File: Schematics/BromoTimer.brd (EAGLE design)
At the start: 49.2 x 71.1 mm, 27 parts, among them IC1 PIC16F687, IC2 7805TV, K1 351, K2 351, Q1 2N3565, Q2 2N3565, Q3 2N3565, X4 22-23-2031, X5 BUZZER

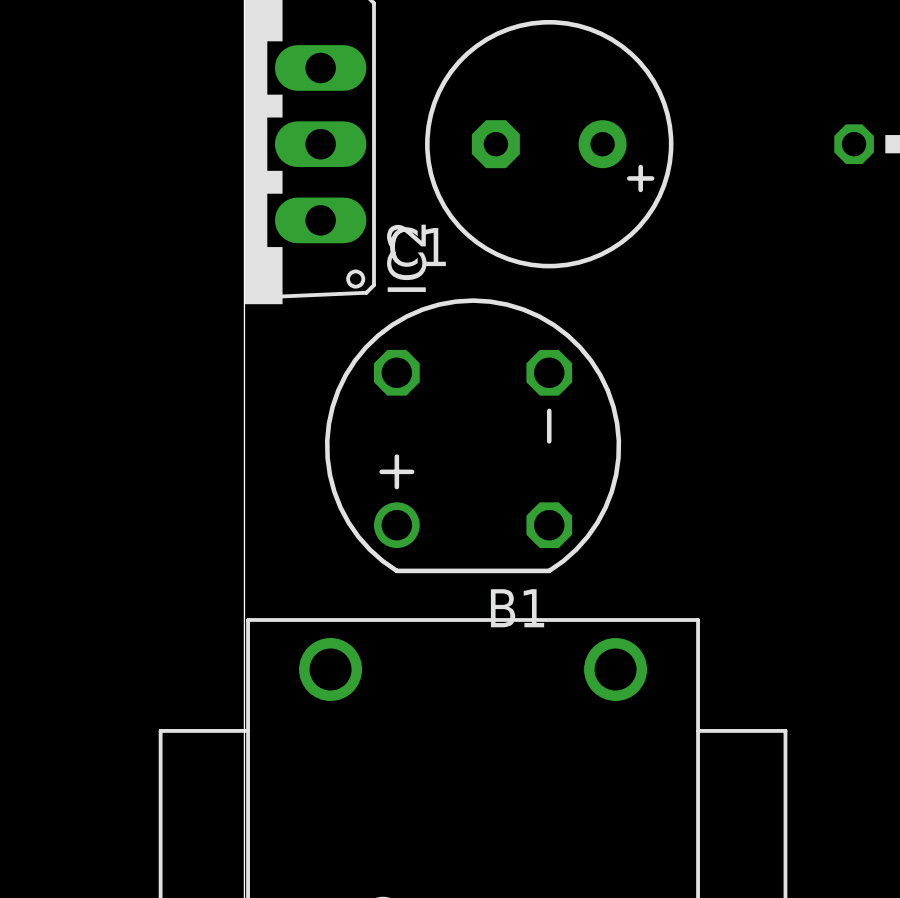
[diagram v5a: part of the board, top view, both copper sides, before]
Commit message: Add 1n4004 diode
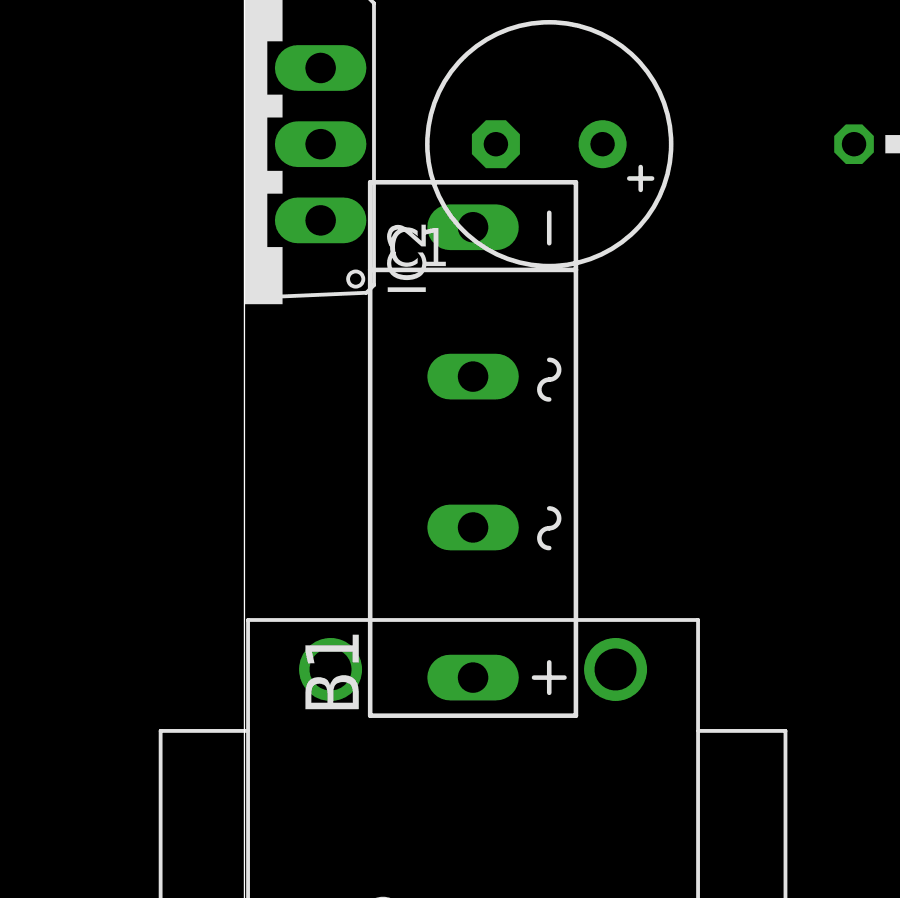
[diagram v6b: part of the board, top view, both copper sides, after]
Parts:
- B1: device rectifier:RB1A -> rectifier:2KBB-R
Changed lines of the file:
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@@
 </element>
 <element name="U$1" library="SparkFun" package="TRANSFORMER" value="TRANSFORMERPTH" x="7.62" y="19.05" rot="R90"/>
-<element name="B1" library="rectifier" package="RB1A" value="" x="7.62" y="31.75" rot="R90"/>
+<element name="B1" library="rectifier" package="2KBB-R" value="" x="7.62" y="31.75" rot="R90"/>
 <element name="D1" library="diode" package="DO35-7" value="1N4148DO35-7" x="3.81" y="-6.35"/>
 <element name="D2" library="diode" package="DO35-7" value="1N4148DO35-7" x="3.81" y="-12.7"/>
@@
 <wire x1="44.45" y1="36.83" x2="42.545" y2="50.8" width="0" layer="19" extent="1-1"/>
 <wire x1="29.21" y1="36.83" x2="44.45" y2="36.83" width="0" layer="19" extent="1-1"/>
-<wire x1="10.16" y1="34.29" x2="29.21" y2="36.83" width="0" layer="19" extent="1-1"/>
-<wire x1="8.382" y1="41.91" x2="10.16" y2="34.29" width="0" layer="19" extent="1-1"/>
+<wire x1="7.62" y1="39.1414" x2="29.21" y2="36.83" width="0" layer="19" extent="1-1"/>
+<wire x1="8.382" y1="41.91" x2="7.62" y2="39.1414" width="0" layer="19" extent="1-1"/>
 <wire x1="2.54" y1="41.91" x2="8.382" y2="41.91" width="0" layer="19" extent="1-1"/>
 <wire x1="5.08" y1="50.8" x2="2.54" y2="41.91" width="0" layer="19" extent="1-1"/>
@@
 <wire x1="19.05" y1="67.31" x2="12.7" y2="52.07" width="0" layer="19" extent="1-1"/>
 <wire x1="2.54" y1="67.31" x2="19.05" y2="67.31" width="0" layer="19" extent="1-1"/>
-<wire x1="7.62" y1="-6.35" x2="10.16" y2="34.29" width="0" layer="19" extent="1-1"/>
+<wire x1="7.62" y1="-6.35" x2="7.62" y2="39.1414" width="0" layer="19" extent="1-1"/>
 <wire x1="7.62" y1="-12.7" x2="7.62" y2="-6.35" width="0" layer="19" extent="1-1"/>
 <wire x1="5.08" y1="-20.32" x2="7.62" y2="-12.7" width="0" layer="19" extent="1-1"/>
@@
 <contactref element="U$1" pad="3"/>
 <contactref element="B1" pad="AC2"/>
-<wire x1="12.37" y1="24.4" x2="10.16" y2="29.21" width="0" layer="19" extent="1-1"/>
+<wire x1="12.37" y1="24.4" x2="7.62" y2="34.163" width="0" layer="19" extent="1-1"/>
 </signal>
 <signal name="N$12">
 <contactref element="B1" pad="AC1"/>
 <contactref element="U$1" pad="4"/>
-<wire x1="2.87" y1="24.4" x2="5.08" y2="34.29" width="0" layer="19" extent="1-1"/>
+<wire x1="2.87" y1="24.4" x2="7.62" y2="29.1338" width="0" layer="19" extent="1-1"/>
 </signal>
 <signal name="V+">
@@
 <wire x1="11.938" y1="41.91" x2="26.67" y2="31.75" width="0" layer="19" extent="1-1"/>
 <wire x1="2.54" y1="39.37" x2="11.938" y2="41.91" width="0" layer="19" extent="1-1"/>
-<wire x1="5.08" y1="29.21" x2="2.54" y2="39.37" width="0" layer="19" extent="1-1"/>
-<wire x1="0" y1="-6.35" x2="5.08" y2="29.21" width="0" layer="19" extent="1-1"/>
+<wire x1="7.62" y1="24.13" x2="2.54" y2="39.37" width="0" layer="19" extent="1-1"/>
+<wire x1="0" y1="-6.35" x2="7.62" y2="24.13" width="0" layer="19" extent="1-1"/>
 <wire x1="0" y1="-12.7" x2="0" y2="-6.35" width="0" layer="19" extent="1-1"/>
 <wire x1="0" y1="-27.94" x2="0" y2="-12.7" width="0" layer="19" extent="1-1"/>

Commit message: Fix bug in relay protection
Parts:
- D3: value 1N4148DO35-7 -> 1N4004; device diode:DO35-7 -> diode:DO41-10
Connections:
- net GND: no longer D1.A, D2.A
- net N$6: now also D1.A
- net N$7: now also D2.A
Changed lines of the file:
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@@
 <attribute name="OC_FARNELL" value="unknown" x="5.08" y="-20.32" size="1.778" layer="27" display="off"/>
 </element>
-<element name="D3" library="diode" package="DO35-7" value="1N4148DO35-7" x="3.81" y="-27.94"/>
+<element name="D3" library="diode" package="DO41-10" value="1N4004" x="3.81" y="-27.94"/>
 <element name="Q3" library="transistor-npn" package="TO92" value="2N3565" x="0" y="-34.29"/>
 <element name="R5" library="rcl" package="0207/10" value="" x="3.81" y="-39.37"/>
@@
 <wire x1="2.54" y1="44.45" x2="2.54" y2="50.8" width="0" layer="19" extent="1-1"/>
 <wire x1="2.54" y1="-20.32" x2="2.54" y2="44.45" width="0" layer="19" extent="1-1"/>
-<wire x1="7.62" y1="-27.94" x2="2.54" y2="-20.32" width="0" layer="19" extent="1-1"/>
+<wire x1="8.89" y1="-27.94" x2="2.54" y2="-20.32" width="0" layer="19" extent="1-1"/>
 </signal>
 <signal name="GND">
@@
 <contactref element="SV1" pad="1"/>
 <contactref element="B1" pad="-"/>
-<contactref element="D2" pad="A"/>
-<contactref element="D1" pad="A"/>
 <contactref element="SV3" pad="3"/>
 <contactref element="Q3" pad="1"/>
@@
 <wire x1="44.45" y1="36.83" x2="42.545" y2="50.8" width="0" layer="19" extent="1-1"/>
 <wire x1="29.21" y1="36.83" x2="44.45" y2="36.83" width="0" layer="19" extent="1-1"/>
-<wire x1="7.62" y1="39.1414" x2="29.21" y2="36.83" width="0" layer="19" extent="1-1"/>
-<wire x1="8.382" y1="41.91" x2="7.62" y2="39.1414" width="0" layer="19" extent="1-1"/>
-<wire x1="2.54" y1="41.91" x2="8.382" y2="41.91" width="0" layer="19" extent="1-1"/>
+<wire x1="8.382" y1="41.91" x2="29.21" y2="36.83" width="0" layer="19" extent="1-1"/>
+<wire x1="7.62" y1="39.1414" x2="8.382" y2="41.91" width="0" layer="19" extent="1-1"/>
+<wire x1="2.54" y1="41.91" x2="7.62" y2="39.1414" width="0" layer="19" extent="1-1"/>
 <wire x1="5.08" y1="50.8" x2="2.54" y2="41.91" width="0" layer="19" extent="1-1"/>
 <wire x1="12.7" y1="52.07" x2="5.08" y2="50.8" width="0" layer="19" extent="1-1"/>
 <wire x1="19.05" y1="67.31" x2="12.7" y2="52.07" width="0" layer="19" extent="1-1"/>
 <wire x1="2.54" y1="67.31" x2="19.05" y2="67.31" width="0" layer="19" extent="1-1"/>
-<wire x1="7.62" y1="-6.35" x2="7.62" y2="39.1414" width="0" layer="19" extent="1-1"/>
-<wire x1="7.62" y1="-12.7" x2="7.62" y2="-6.35" width="0" layer="19" extent="1-1"/>
-<wire x1="5.08" y1="-20.32" x2="7.62" y2="-12.7" width="0" layer="19" extent="1-1"/>
+<wire x1="5.08" y1="-20.32" x2="7.62" y2="39.1414" width="0" layer="19" extent="1-1"/>
 <wire x1="1.27" y1="-34.29" x2="5.08" y2="-20.32" width="0" layer="19" extent="1-1"/>
 <wire x1="-11.43" y1="-34.29" x2="1.27" y2="-34.29" width="0" layer="19" extent="1-1"/>
@@
 <contactref element="Q2" pad="1"/>
 <contactref element="K2" pad="16"/>
-<wire x1="31.75" y1="36.83" x2="34.29" y2="31.75" width="0" layer="19" extent="1-1"/>
+<contactref element="D1" pad="A"/>
+<wire x1="34.29" y1="31.75" x2="31.75" y2="36.83" width="0" layer="19" extent="1-1"/>
+<wire x1="7.62" y1="-6.35" x2="34.29" y2="31.75" width="0" layer="19" extent="1-1"/>
 </signal>
 <signal name="N$7">
 <contactref element="Q1" pad="1"/>
 <contactref element="K1" pad="16"/>
-<wire x1="46.99" y1="36.83" x2="46.99" y2="31.75" width="0" layer="19" extent="1-1"/>
+<contactref element="D2" pad="A"/>
+<wire x1="46.99" y1="31.75" x2="46.99" y2="36.83" width="0" layer="19" extent="1-1"/>
+<wire x1="7.62" y1="-12.7" x2="46.99" y2="31.75" width="0" layer="19" extent="1-1"/>
 </signal>
 <signal name="N$8">
@@
 <wire x1="0" y1="-6.35" x2="7.62" y2="24.13" width="0" layer="19" extent="1-1"/>
 <wire x1="0" y1="-12.7" x2="0" y2="-6.35" width="0" layer="19" extent="1-1"/>
-<wire x1="0" y1="-27.94" x2="0" y2="-12.7" width="0" layer="19" extent="1-1"/>
-<wire x1="-5.08" y1="-34.29" x2="0" y2="-27.94" width="0" layer="19" extent="1-1"/>
+<wire x1="-1.27" y1="-27.94" x2="0" y2="-12.7" width="0" layer="19" extent="1-1"/>
+<wire x1="-5.08" y1="-34.29" x2="-1.27" y2="-27.94" width="0" layer="19" extent="1-1"/>
 </signal>
 <signal name="N$16">

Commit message: Add on-board buzzer
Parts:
- removed X5: BUZZER, con-molex:22-23-2021
- added SG1: EB2209A, buzzer:EB2209A
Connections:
- net GND: now also Q3.3; no longer Q3.1
- net N$19: now also Q3.1, SG1.-; no longer Q3.3, X5.1
- net V+: now also SG1.+; no longer X5.2
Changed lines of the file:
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@@
 <element name="Q3" library="transistor-npn" package="TO92" value="2N3565" x="0" y="-34.29"/>
 <element name="R5" library="rcl" package="0207/10" value="" x="3.81" y="-39.37"/>
-<element name="X5" library="con-molex" package="22-23-2021" value="BUZZER" x="-6.35" y="-34.29">
-<attribute name="OC_NEWARK" value="25C3832" x="-6.35" y="-34.29" size="1.778" layer="27" display="off"/>
-<attribute name="MPN" value="22-23-2021" x="-6.35" y="-34.29" size="1.778" layer="27" display="off"/>
-<attribute name="MF" value="MOLEX" x="-6.35" y="-34.29" size="1.778" layer="27" display="off"/>
-<attribute name="OC_FARNELL" value="1462926" x="-6.35" y="-34.29" size="1.778" layer="27" display="off"/>
-</element>
 <element name="X4" library="con-molex" package="22-23-2031" value="22-23-2031" x="-13.97" y="-34.29">
 <attribute name="OC_NEWARK" value="30C0862" x="-13.97" y="-34.29" size="1.778" layer="27" display="off"/>
@@
 <attribute name="MF" value="MOLEX" x="-13.97" y="-34.29" size="1.778" layer="27" display="off"/>
 <attribute name="OC_FARNELL" value="1462950" x="-13.97" y="-34.29" size="1.778" layer="27" display="off"/>
+</element>
+<element name="SG1" library="buzzer" package="EB2209A" value="EB2209A" x="-6.35" y="-54.61">
+<attribute name="OC_NEWARK" value="unknown" x="-6.35" y="-54.61" size="1.778" layer="27" display="off"/>
+<attribute name="MPN" value="" x="-6.35" y="-54.61" size="1.778" layer="27" display="off"/>
+<attribute name="MF" value="" x="-6.35" y="-54.61" size="1.778" layer="27" display="off"/>
+<attribute name="OC_FARNELL" value="unknown" x="-6.35" y="-54.61" size="1.778" layer="27" display="off"/>
 </element>
 </elements>
@@
 <contactref element="B1" pad="-"/>
 <contactref element="SV3" pad="3"/>
-<contactref element="Q3" pad="1"/>
 <contactref element="X4" pad="3"/>
+<contactref element="Q3" pad="3"/>
 <wire x1="42.545" y1="50.8" x2="46.99" y2="67.31" width="0" layer="19" extent="1-1"/>
 <wire x1="44.45" y1="36.83" x2="42.545" y2="50.8" width="0" layer="19" extent="1-1"/>
@@
 <wire x1="2.54" y1="67.31" x2="19.05" y2="67.31" width="0" layer="19" extent="1-1"/>
 <wire x1="5.08" y1="-20.32" x2="7.62" y2="39.1414" width="0" layer="19" extent="1-1"/>
-<wire x1="1.27" y1="-34.29" x2="5.08" y2="-20.32" width="0" layer="19" extent="1-1"/>
-<wire x1="-11.43" y1="-34.29" x2="1.27" y2="-34.29" width="0" layer="19" extent="1-1"/>
+<wire x1="-1.27" y1="-34.29" x2="5.08" y2="-20.32" width="0" layer="19" extent="1-1"/>
+<wire x1="-11.43" y1="-34.29" x2="-1.27" y2="-34.29" width="0" layer="19" extent="1-1"/>
 </signal>
 <signal name="RS">
@@
 <contactref element="D1" pad="C"/>
 <contactref element="D3" pad="C"/>
-<contactref element="X5" pad="2"/>
+<contactref element="SG1" pad="+"/>
 <wire x1="26.67" y1="31.75" x2="39.37" y2="31.75" width="0" layer="19" extent="1-1"/>
 <wire x1="11.938" y1="41.91" x2="26.67" y2="31.75" width="0" layer="19" extent="1-1"/>
@@
 <wire x1="0" y1="-12.7" x2="0" y2="-6.35" width="0" layer="19" extent="1-1"/>
 <wire x1="-1.27" y1="-27.94" x2="0" y2="-12.7" width="0" layer="19" extent="1-1"/>
-<wire x1="-5.08" y1="-34.29" x2="-1.27" y2="-27.94" width="0" layer="19" extent="1-1"/>
+<wire x1="1.143" y1="-54.61" x2="-1.27" y2="-27.94" width="0" layer="19" extent="1-1"/>
 </signal>
 <signal name="N$16">
@@
 <wire x1="8.89" y1="-39.37" x2="22.86" y2="52.07" width="0" layer="19" extent="1-1"/>
 </signal>
-<signal name="N$18">
-<contactref element="R5" pad="1"/>
-<contactref element="Q3" pad="2"/>
-<wire x1="0" y1="-32.385" x2="-1.27" y2="-39.37" width="0" layer="19" extent="1-1"/>
-</signal>
-<signal name="N$19">
-<contactref element="Q3" pad="3"/>
-<contactref element="X5" pad="1"/>
-<wire x1="-1.27" y1="-34.29" x2="-7.62" y2="-34.29" width="0" layer="19" extent="1-1"/>
-</signal>
 <signal name="N$13">
 <contactref element="IC1" pad="17"/>
@@
 <wire x1="-16.51" y1="-34.29" x2="17.78" y2="52.07" width="0" layer="19" extent="1-1"/>
 </signal>
+<signal name="N$18">
+<contactref element="Q3" pad="2"/>
+<contactref element="R5" pad="1"/>
+<wire x1="0" y1="-32.385" x2="-1.27" y2="-39.37" width="0" layer="19" extent="1-1"/>
+</signal>
+<signal name="N$19">
+<contactref element="Q3" pad="1"/>
+<contactref element="SG1" pad="-"/>
+<wire x1="1.27" y1="-34.29" x2="-13.843" y2="-54.61" width="0" layer="19" extent="1-1"/>
+</signal>
 </signals>
